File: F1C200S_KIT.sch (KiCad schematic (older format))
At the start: 0 parts

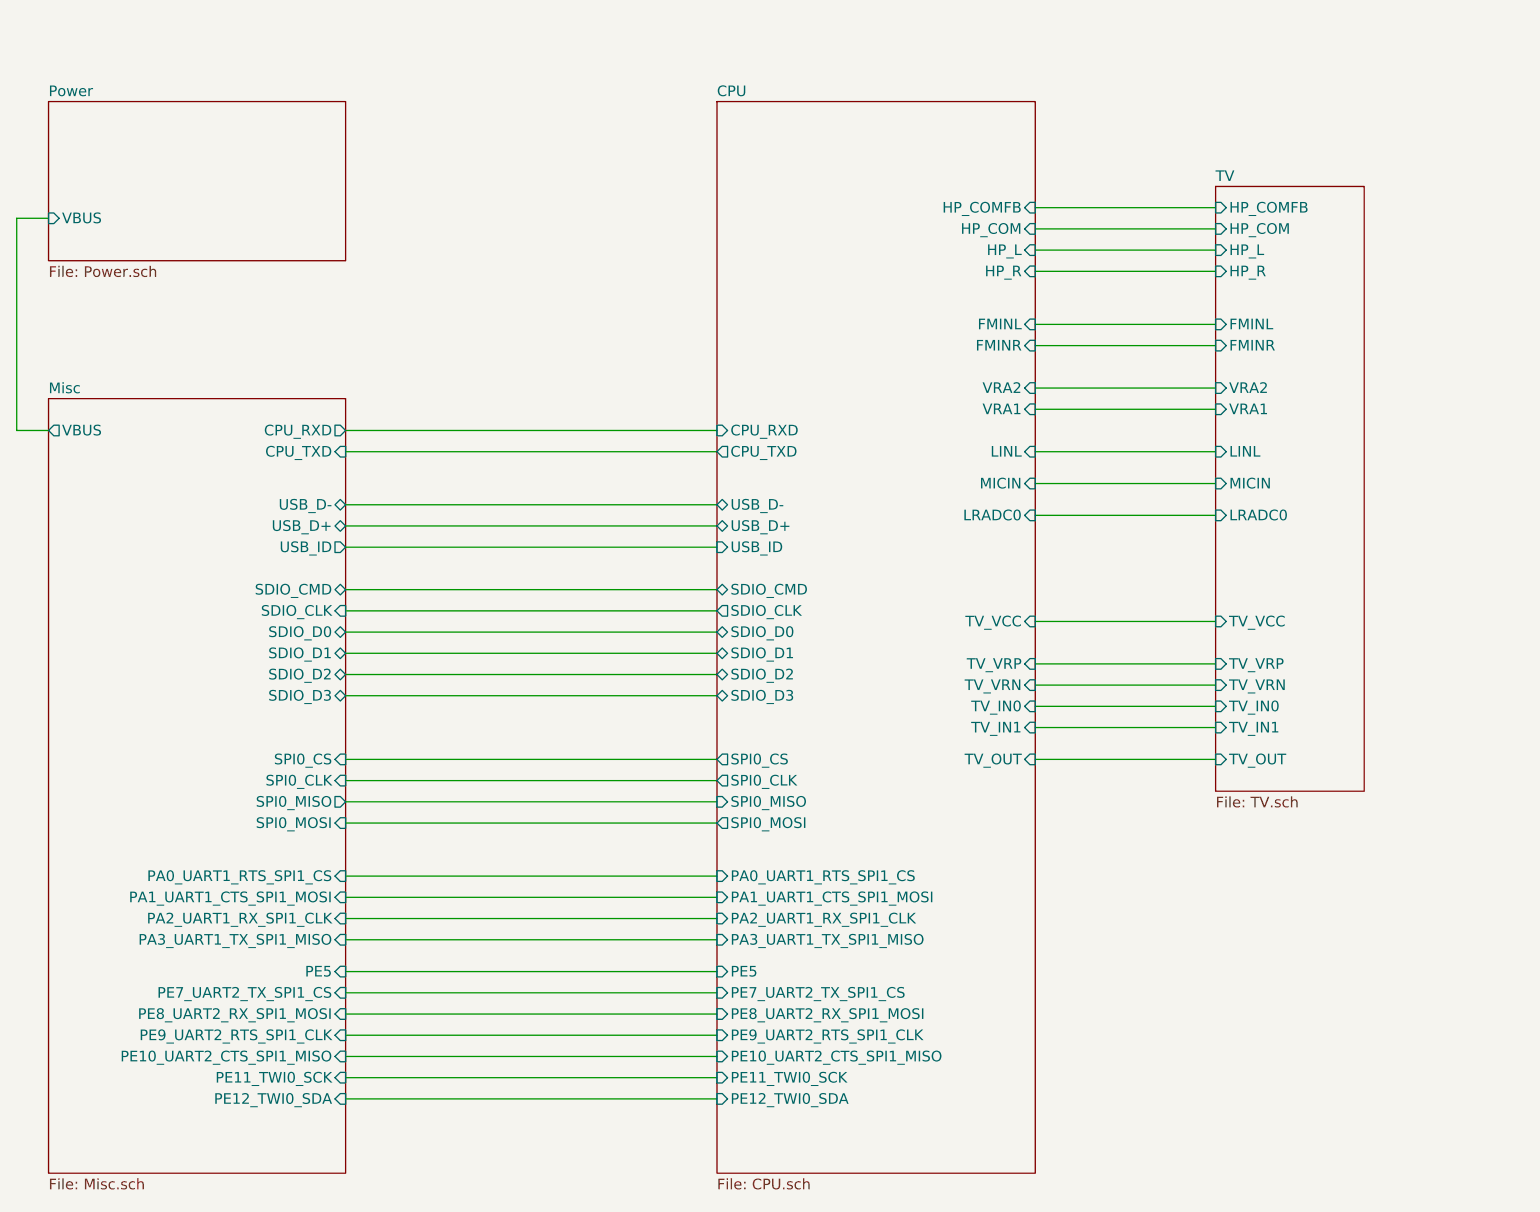
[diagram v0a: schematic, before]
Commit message: Removed TV. Added USB. Refactored.
Signed-off-by: Sebastian Basierski <sebastian@basierski.pl>
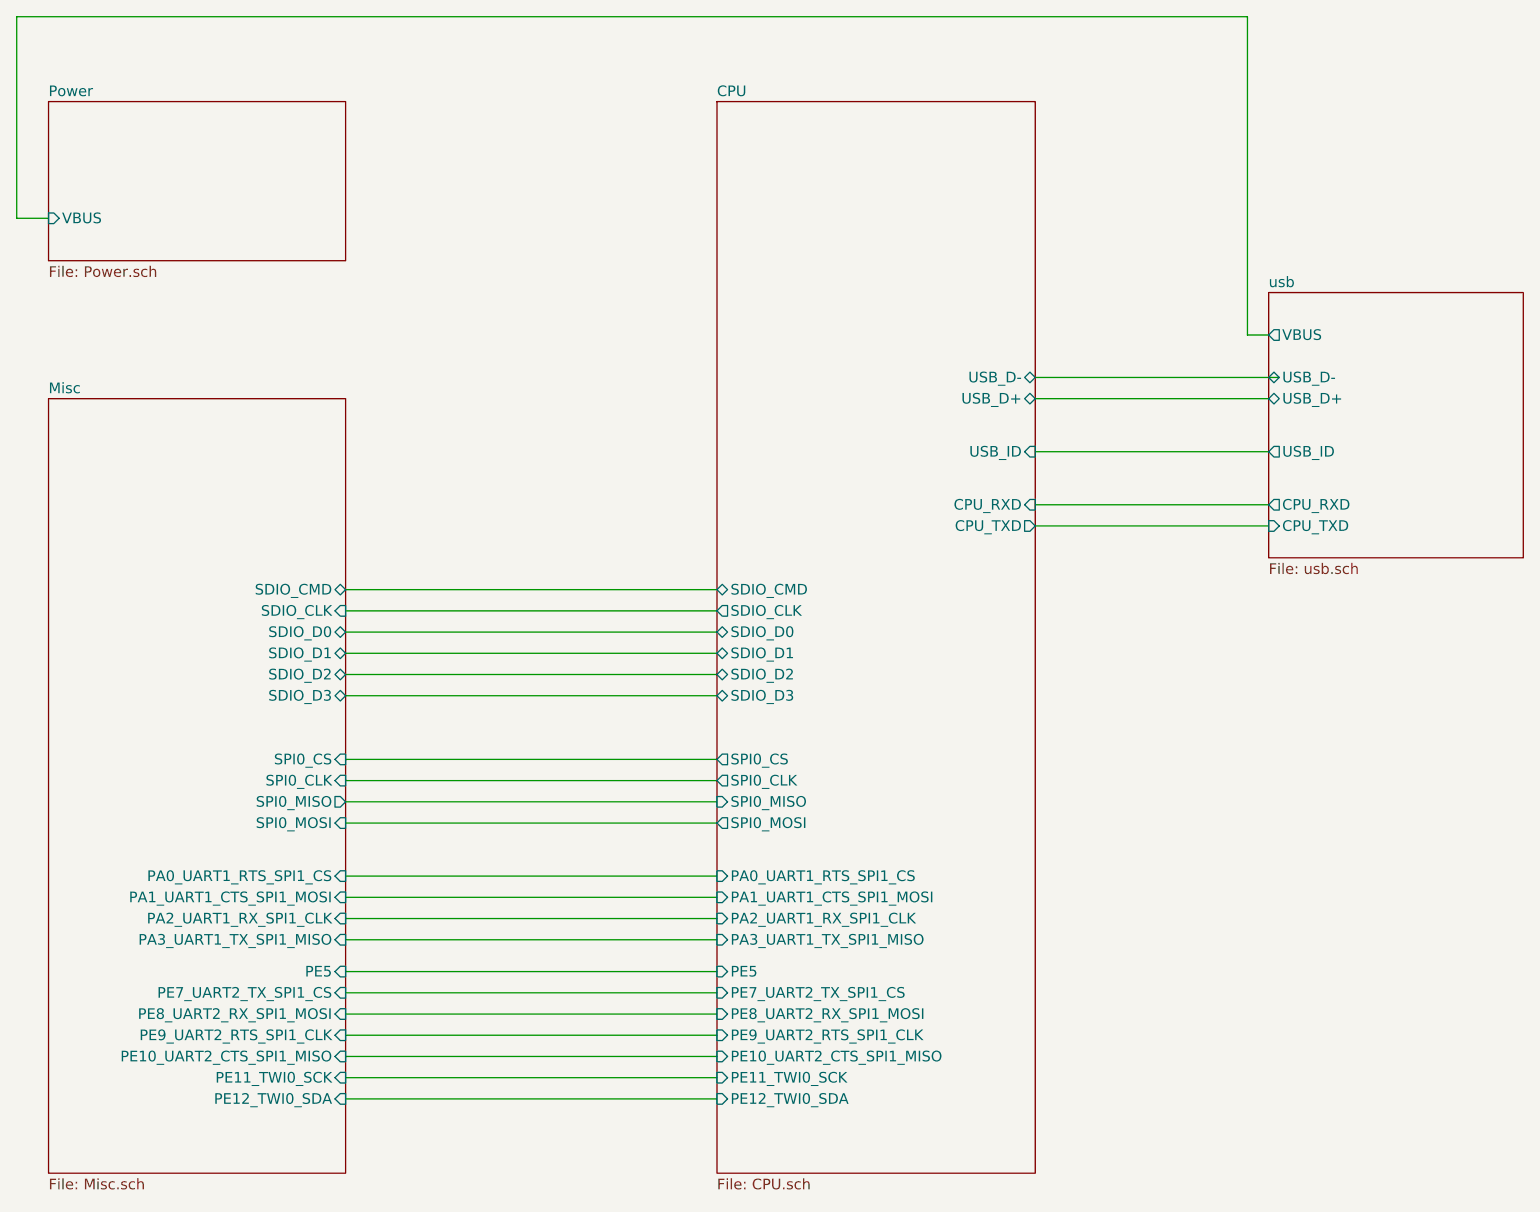
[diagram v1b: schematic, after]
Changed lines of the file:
@@
-EESchema Schematic File Version 4
+EESchema Schematic File Version 5
 EELAYER 30 0
 EELAYER END
@@
 Comment3 ""
 Comment4 ""
+Comment5 ""
+Comment6 ""
+Comment7 ""
+Comment8 ""
+Comment9 ""
 $EndDescr
-$Sheet
-S 5350 1100 1500 5050
-U 5E3A4A8E
-F0 "CPU" 50
-F1 "CPU.sch" 50
-F2 "USB_D-" B L 5350 3000 50
-F3 "USB_D+" B L 5350 3100 50
-F4 "CPU_RXD" I L 5350 2650 50
-F5 "CPU_TXD" O L 5350 2750 50
-F6 "USB_ID" I L 5350 3200 50
-F7 "SDIO_CLK" O L 5350 3500 50
-F8 "SDIO_D2" B L 5350 3800 50
-F9 "SDIO_D3" B L 5350 3900 50
-F10 "SDIO_CMD" B L 5350 3400 50
-F11 "SDIO_D0" B L 5350 3600 50
-F12 "SDIO_D1" B L 5350 3700 50
-F13 "SPI0_CS" O L 5350 4200 50
-F14 "SPI0_CLK" O L 5350 4300 50
-F15 "SPI0_MISO" I L 5350 4400 50
-F16 "SPI0_MOSI" O L 5350 4500 50
-F17 "HP_L" I R 6850 1800 50
-F18 "HP_R" I R 6850 1900 50
-F19 "HP_COM" I R 6850 1700 50
-F20 "VRA1" I R 6850 2550 50
-F21 "VRA2" I R 6850 2450 50
-F22 "FMINL" I R 6850 2150 50
-F23 "FMINR" I R 6850 2250 50
-F24 "LINL" I R 6850 2750 50
-F25 "MICIN" I R 6850 2900 50
-F26 "LRADC0" I R 6850 3050 50
-F27 "TV_IN0" I R 6850 3950 50
-F28 "TV_IN1" I R 6850 4050 50
-F29 "TV_VRP" I R 6850 3750 50
-F30 "TV_VRN" I R 6850 3850 50
-F31 "TV_VCC" I R 6850 3550 50
-F32 "TV_OUT" I R 6850 4200 50
-F33 "PA0_UART1_RTS_SPI1_CS" I L 5350 4750 50
-F34 "PA1_UART1_CTS_SPI1_MOSI" I L 5350 4850 50
-F35 "PA2_UART1_RX_SPI1_CLK" I L 5350 4950 50
-F36 "PA3_UART1_TX_SPI1_MISO" I L 5350 5050 50
-F37 "PE7_UART2_TX_SPI1_CS" I L 5350 5300 50
-F38 "PE8_UART2_RX_SPI1_MOSI" I L 5350 5400 50
-F39 "PE9_UART2_RTS_SPI1_CLK" I L 5350 5500 50
-F40 "PE10_UART2_CTS_SPI1_MISO" I L 5350 5600 50
-F41 "PE12_TWI0_SDA" I L 5350 5800 50
-F42 "PE11_TWI0_SCK" I L 5350 5700 50
-F43 "PE5" I L 5350 5200 50
-F44 "HP_COMFB" I R 6850 1600 50
-$EndSheet
 Wire Wire Line
-	2200 2650 2050 2650
-Wire Wire Line
-	2050 2650 2050 1650
-Wire Wire Line
-	2050 1650 2200 1650
-$Sheet
-S 2200 1100 1400 750
-U 5E3A4AC6
-F0 "Power" 50
-F1 "Power.sch" 50
-F2 "VBUS" I L 2200 1650 50
-$EndSheet
-$Sheet
-S 2200 2500 1400 3650
-U 5E3A651C
-F0 "Misc" 50
-F1 "Misc.sch" 50
-F2 "CPU_RXD" O R 3600 2650 50
-F3 "CPU_TXD" I R 3600 2750 50
-F4 "VBUS" O L 2200 2650 50
-F5 "USB_D-" B R 3600 3000 50
-F6 "USB_D+" B R 3600 3100 50
-F7 "SDIO_CLK" I R 3600 3500 50
-F8 "SDIO_D0" B R 3600 3600 50
-F9 "SDIO_D3" B R 3600 3900 50
-F10 "SDIO_CMD" B R 3600 3400 50
-F11 "SDIO_D1" B R 3600 3700 50
-F12 "USB_ID" O R 3600 3200 50
-F13 "SDIO_D2" B R 3600 3800 50
-F14 "SPI0_CS" I R 3600 4200 50
-F15 "SPI0_CLK" I R 3600 4300 50
-F16 "SPI0_MISO" O R 3600 4400 50
-F17 "SPI0_MOSI" I R 3600 4500 50
-F18 "PE7_UART2_TX_SPI1_CS" I R 3600 5300 50
-F19 "PE8_UART2_RX_SPI1_MOSI" I R 3600 5400 50
-F20 "PE9_UART2_RTS_SPI1_CLK" I R 3600 5500 50
-F21 "PE10_UART2_CTS_SPI1_MISO" I R 3600 5600 50
-F22 "PA0_UART1_RTS_SPI1_CS" I R 3600 4750 50
-F23 "PA1_UART1_CTS_SPI1_MOSI" I R 3600 4850 50
-F24 "PA2_UART1_RX_SPI1_CLK" I R 3600 4950 50
-F25 "PA3_UART1_TX_SPI1_MISO" I R 3600 5050 50
-F26 "PE11_TWI0_SCK" I R 3600 5700 50
-F27 "PE12_TWI0_SDA" I R 3600 5800 50
-F28 "PE5" I R 3600 5200 50
-$EndSheet
-Wire Wire Line
-	3600 2650 5350 2650
-Wire Wire Line
-	3600 2750 5350 2750
-Wire Wire Line
-	3600 3000 5350 3000
-Wire Wire Line
-	3600 3100 5350 3100
-Wire Wire Line
-	3600 3200 5350 3200
+	3600 3600 5350 3600
 Wire Wire Line
 	3600 3400 5350 3400
@@
 	3600 3500 5350 3500
 Wire Wire Line
-	3600 3600 5350 3600
+	6850 3100 7950 3100
+Wire Wire Line
+	2050 700  7850 700
+Wire Wire Line
+	7850 700  7850 2200
+$Sheet
+S 7950 2000 1200 1250
+U 5F1F2557
+F0 "usb" 50
+F1 "usb.sch" 50
+F2 "VBUS" O L 7950 2200 50
+F3 "USB_ID" O L 7950 2750 50
+F4 "USB_D+" B L 7950 2500 50
+F5 "USB_D-" B L 7950 2400 50
+F6 "CPU_RXD" O L 7950 3000 50
+F7 "CPU_TXD" I L 7950 3100 50
+$EndSheet
+Wire Wire Line
+	6850 3000 7950 3000
+Wire Wire Line
+	6850 2750 7950 2750
+Wire Wire Line
+	6850 2400 8000 2400
+Wire Wire Line
+	6850 2500 7950 2500
+Wire Wire Line
+	7850 2200 7950 2200
 Wire Wire Line
 	3600 3700 5350 3700
@@
 	3600 4200 5350 4200
 Wire Wire Line
-	3600 4300 5350 4300
-Wire Wire Line
-	3600 4400 5350 4400
-Wire Wire Line
-	3600 4500 5350 4500
-$Sheet
-S 7700 1500 700  2850
-U 5E5BEA7B
-F0 "TV" 50
-F1 "TV.sch" 50
-F2 "HP_L" I L 7700 1800 50
-F3 "HP_COM" I L 7700 1700 50
-F4 "HP_R" I L 7700 1900 50
-F5 "MICIN" I L 7700 2900 50
-F6 "LINL" I L 7700 2750 50
-F7 "FMINR" I L 7700 2250 50
-F8 "FMINL" I L 7700 2150 50
-F9 "VRA2" I L 7700 2450 50
-F10 "VRA1" I L 7700 2550 50
-F11 "LRADC0" I L 7700 3050 50
-F12 "TV_IN0" I L 7700 3950 50
-F13 "TV_IN1" I L 7700 4050 50
-F14 "TV_VRP" I L 7700 3750 50
-F15 "TV_VRN" I L 7700 3850 50
-F16 "TV_VCC" I L 7700 3550 50
-F17 "TV_OUT" I L 7700 4200 50
-F18 "HP_COMFB" I L 7700 1600 50
-$EndSheet
-Wire Wire Line
-	5350 5300 3600 5300
-Wire Wire Line
 	5350 4750 3600 4750
-Wire Wire Line
-	5350 5200 3600 5200
 Wire Wire Line
 	5350 5400 3600 5400
@@
 	5350 5800 3600 5800
 Wire Wire Line
+	5350 5300 3600 5300
+Wire Wire Line
+	5350 5200 3600 5200
+Wire Wire Line
 	3600 4850 5350 4850
 Wire Wire Line
@@
 	3600 5050 5350 5050
 Wire Wire Line
-	6850 1600 7700 1600
+	3600 4300 5350 4300
 Wire Wire Line
-	6850 2150 7700 2150
+	3600 4400 5350 4400
 Wire Wire Line
-	6850 2450 7700 2450
+	3600 4500 5350 4500
+$Sheet
+S 5350 1100 1500 5050
+U 5E3A4A8E
+F0 "CPU" 50
+F1 "CPU.sch" 50
+F2 "USB_D-" B R 6850 2400 50
+F3 "USB_D+" B R 6850 2500 50
+F4 "CPU_RXD" I R 6850 3000 50
+F5 "CPU_TXD" O R 6850 3100 50
+F6 "USB_ID" I R 6850 2750 50
+F7 "SDIO_CLK" O L 5350 3500 50
+F8 "SDIO_D2" B L 5350 3800 50
+F9 "SDIO_D3" B L 5350 3900 50
+F10 "SDIO_CMD" B L 5350 3400 50
+F11 "SDIO_D0" B L 5350 3600 50
+F12 "SDIO_D1" B L 5350 3700 50
+F13 "SPI0_CS" O L 5350 4200 50
+F14 "SPI0_CLK" O L 5350 4300 50
+F15 "SPI0_MISO" I L 5350 4400 50
+F16 "SPI0_MOSI" O L 5350 4500 50
+F17 "PA0_UART1_RTS_SPI1_CS" I L 5350 4750 50
+F18 "PA1_UART1_CTS_SPI1_MOSI" I L 5350 4850 50
+F19 "PA2_UART1_RX_SPI1_CLK" I L 5350 4950 50
+F20 "PA3_UART1_TX_SPI1_MISO" I L 5350 5050 50
+F21 "PE7_UART2_TX_SPI1_CS" I L 5350 5300 50
+F22 "PE8_UART2_RX_SPI1_MOSI" I L 5350 5400 50
+F23 "PE9_UART2_RTS_SPI1_CLK" I L 5350 5500 50
+F24 "PE10_UART2_CTS_SPI1_MISO" I L 5350 5600 50
+F25 "PE12_TWI0_SDA" I L 5350 5800 50
+F26 "PE11_TWI0_SCK" I L 5350 5700 50
+F27 "PE5" I L 5350 5200 50
+$EndSheet
+$Sheet
+S 2200 2500 1400 3650
+U 5E3A651C
+F0 "Misc" 50
+F1 "Misc.sch" 50
+F2 "SDIO_CLK" I R 3600 3500 50
+F3 "SDIO_D0" B R 3600 3600 50
+F4 "SDIO_D3" B R 3600 3900 50
+F5 "SDIO_CMD" B R 3600 3400 50
+F6 "SDIO_D1" B R 3600 3700 50
+F7 "SDIO_D2" B R 3600 3800 50
+F8 "SPI0_CS" I R 3600 4200 50
+F9 "SPI0_CLK" I R 3600 4300 50
+F10 "SPI0_MISO" O R 3600 4400 50
+F11 "SPI0_MOSI" I R 3600 4500 50
+F12 "PE7_UART2_TX_SPI1_CS" I R 3600 5300 50
+F13 "PE8_UART2_RX_SPI1_MOSI" I R 3600 5400 50
+F14 "PE9_UART2_RTS_SPI1_CLK" I R 3600 5500 50
+F15 "PE10_UART2_CTS_SPI1_MISO" I R 3600 5600 50
+F16 "PA0_UART1_RTS_SPI1_CS" I R 3600 4750 50
+F17 "PA1_UART1_CTS_SPI1_MOSI" I R 3600 4850 50
+F18 "PA2_UART1_RX_SPI1_CLK" I R 3600 4950 50
+F19 "PA3_UART1_TX_SPI1_MISO" I R 3600 5050 50
+F20 "PE11_TWI0_SCK" I R 3600 5700 50
+F21 "PE12_TWI0_SDA" I R 3600 5800 50
+F22 "PE5" I R 3600 5200 50
+$EndSheet
 Wire Wire Line
-	6850 2750 7700 2750
+	2050 1650 2200 1650
+$Sheet
+S 2200 1100 1400 750
+U 5E3A4AC6
+F0 "Power" 50
+F1 "Power.sch" 50
+F2 "VBUS" I L 2200 1650 50
+$EndSheet
 Wire Wire Line
-	6850 3550 7700 3550
-Wire Wire Line
-	6850 3750 7700 3750
-Wire Wire Line
-	6850 4200 7700 4200
-Wire Wire Line
-	6850 3850 7700 3850
-Wire Wire Line
-	6850 3950 7700 3950
-Wire Wire Line
-	6850 4050 7700 4050
-Wire Wire Line
-	6850 2900 7700 2900
-Wire Wire Line
-	6850 3050 7700 3050
-Wire Wire Line
-	6850 2250 7700 2250
-Wire Wire Line
-	6850 2550 7700 2550
-Wire Wire Line
-	6850 1900 7700 1900
-Wire Wire Line
-	6850 1800 7700 1800
-Wire Wire Line
-	6850 1700 7700 1700
+	2050 1650 2050 700
 $EndSCHEMATC
